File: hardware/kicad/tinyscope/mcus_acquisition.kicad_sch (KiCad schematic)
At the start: 30 parts, among them J5 STM32H743, Q2 NMOS, SW1 SW_SPST, U12 STM32H743VITx, X1 25MHz, X2 32k768

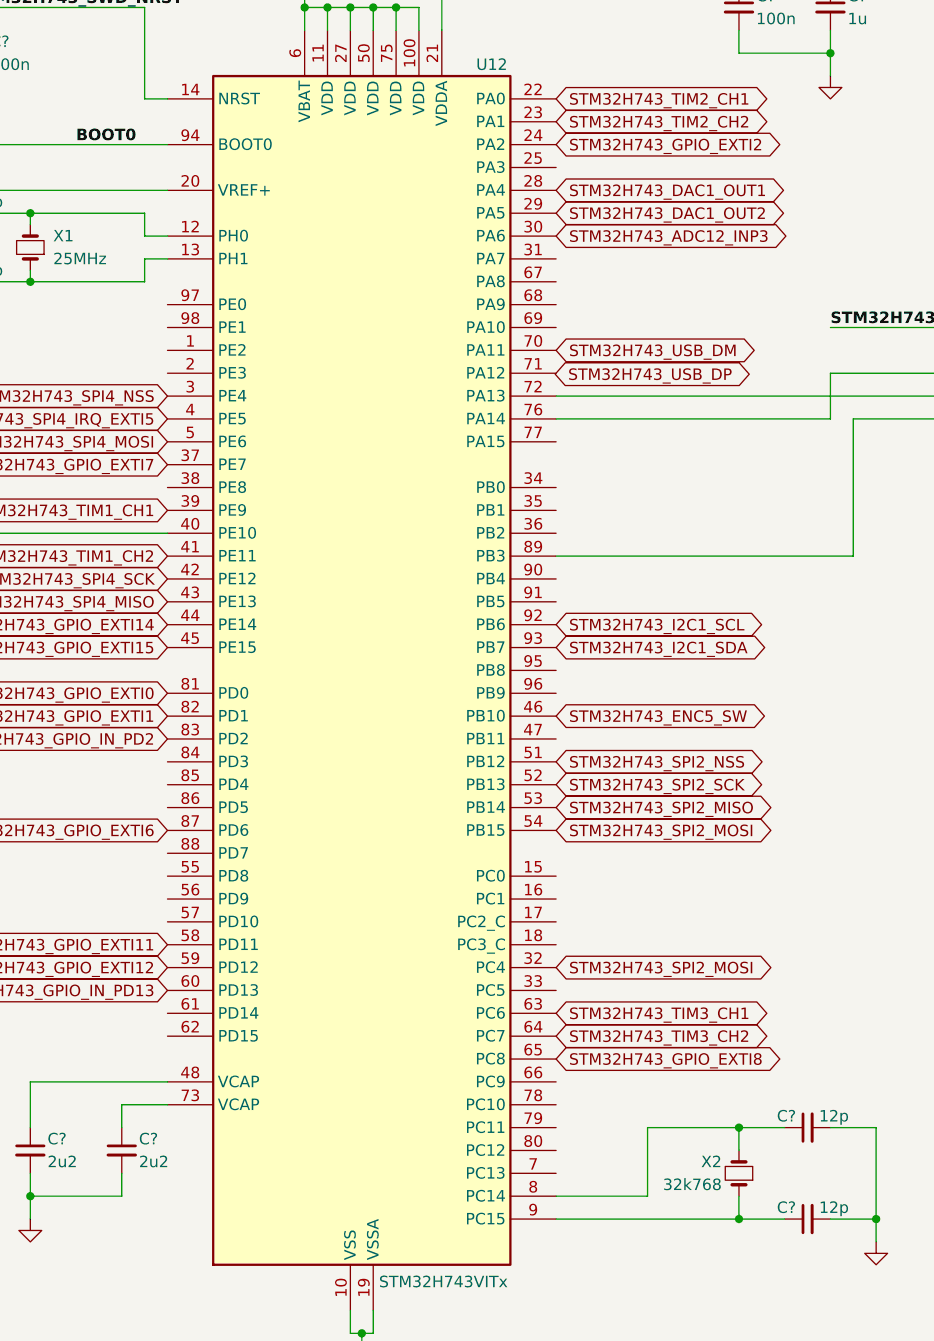
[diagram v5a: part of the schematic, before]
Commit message: feat: hardware: Adds no-connection flags for acquisition mcu
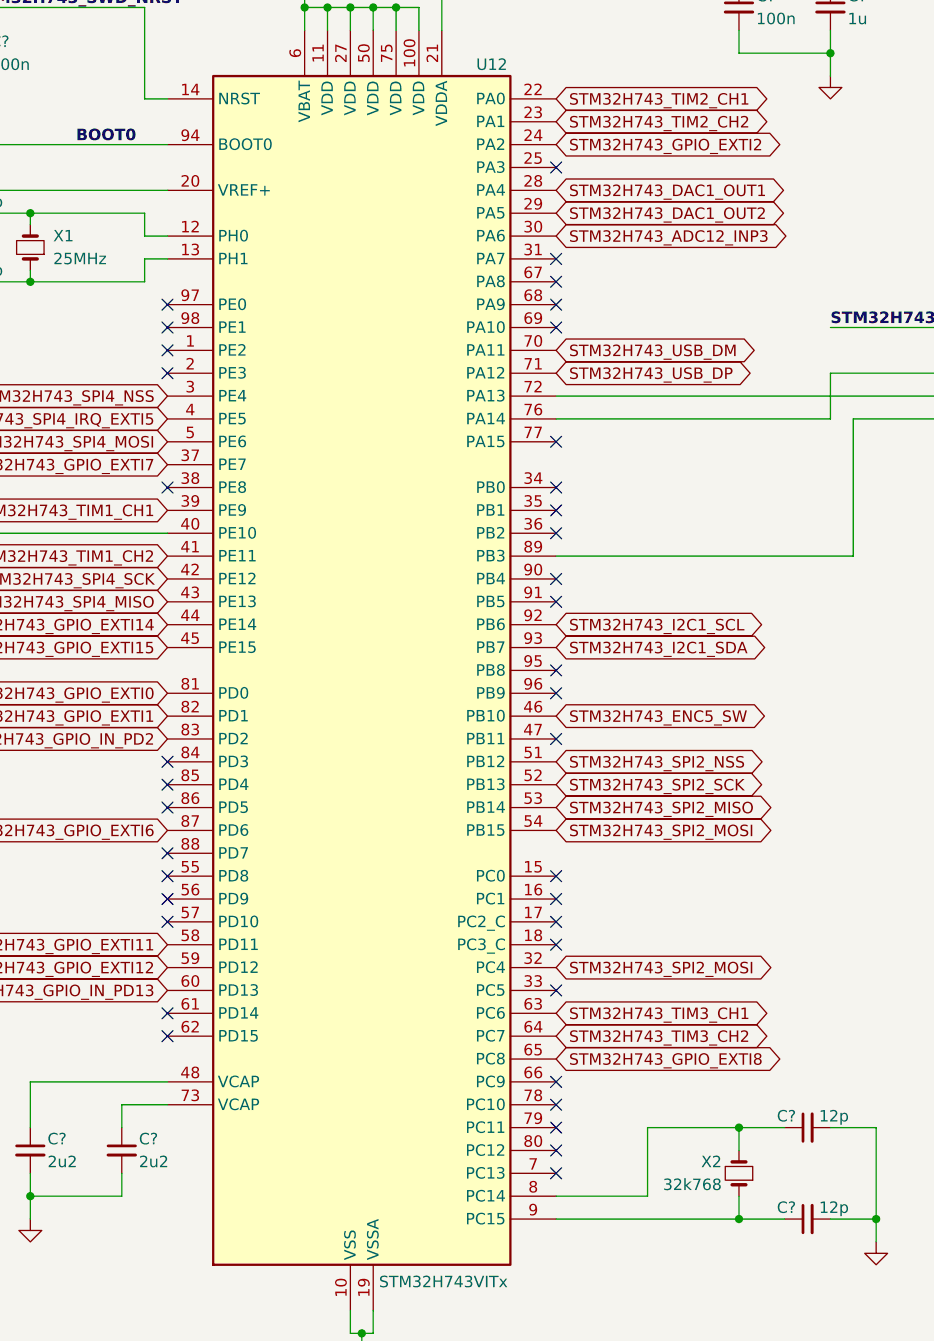
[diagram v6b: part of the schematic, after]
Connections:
- net STM32H743_USB_DP: now also U12.71 (PA12)
- no-connect marks 0 -> 38
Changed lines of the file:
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@@
   (junction (at 104.14 20.32) (diameter 0) (color 0 0 0 0)
   )
+  (no_connect (at 177.8 124.46))
+  (no_connect (at 134.62 66.04))
+  (no_connect (at 177.8 129.54))
+  (no_connect (at 134.62 109.22))
+  (no_connect (at 134.62 121.92))
+  (no_connect (at 134.62 63.5))
+  (no_connect (at 177.8 152.4))
+  (no_connect (at 177.8 55.88))
+  (no_connect (at 177.8 91.44))
+  (no_connect (at 177.8 88.9))
+  (no_connect (at 177.8 147.32))
+  (no_connect (at 177.8 53.34))
+  (no_connect (at 177.8 43.18))
+  (no_connect (at 134.62 137.16))
+  (no_connect (at 134.62 139.7))
+  (no_connect (at 177.8 81.28))
+  (no_connect (at 177.8 154.94))
+  (no_connect (at 177.8 83.82))
+  (no_connect (at 177.8 99.06))
+  (no_connect (at 134.62 78.74))
+  (no_connect (at 177.8 60.96))
+  (no_connect (at 134.62 58.42))
+  (no_connect (at 134.62 114.3))
+  (no_connect (at 177.8 106.68))
+  (no_connect (at 177.8 144.78))
+  (no_connect (at 177.8 149.86))
+  (no_connect (at 177.8 134.62))
+  (no_connect (at 134.62 111.76))
+  (no_connect (at 134.62 127))
+  (no_connect (at 177.8 101.6))
+  (no_connect (at 177.8 121.92))
+  (no_connect (at 177.8 73.66))
+  (no_connect (at 134.62 119.38))
+  (no_connect (at 134.62 124.46))
+  (no_connect (at 177.8 58.42))
+  (no_connect (at 177.8 127))
+  (no_connect (at 177.8 78.74))
+  (no_connect (at 134.62 60.96))
   (wire (pts (xy 63.5 30.48) (xy 63.5 27.94))
     (stroke (width 0) (type default))
@@
     )
   )
-  (global_label "STM32H743_USB_DP" (shape bidirectional) (at 177.6997 66.1468 0) (fields_autoplaced)
-    (effects (font (size 1.27 1.27)) (justify left))
-    (property "Intersheetrefs" "${INTERSHEET_REFS}" (at 201.0085 66.1468 0)
-      (effects (font (size 1.27 1.27)) (justify left) hide)
-    )
+  (global_label "STM32H743_USB_DP" (shape bidirectional) (at 177.8 66.04 0) (fields_autoplaced)
+    (effects (font (size 1.27 1.27)) (justify left))
+    (property "Intersheetrefs" "${INTERSHEET_REFS}" (at 201.1088 66.04 0)
+      (effects (font (size 1.27 1.27)) (justify left) hide)
+    )

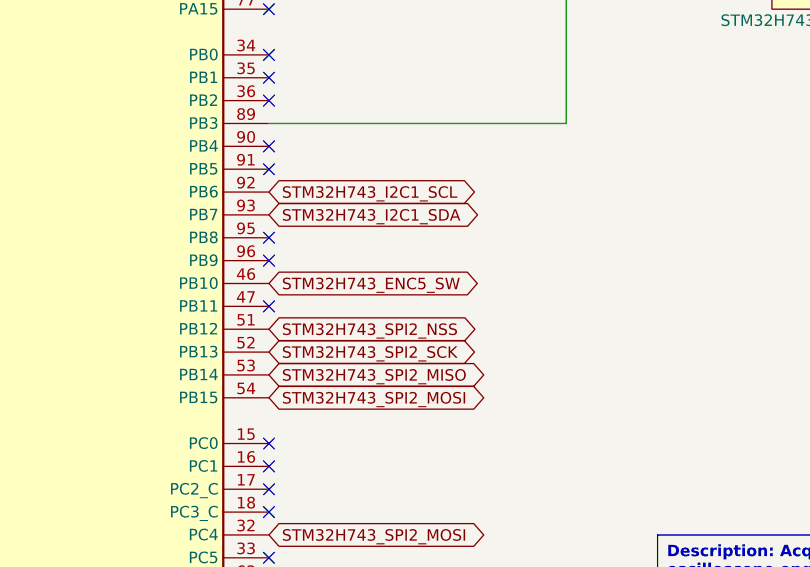
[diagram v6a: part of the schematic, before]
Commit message: feat: hardware: Add global labels on power and charging, and regulation and rails subschematics
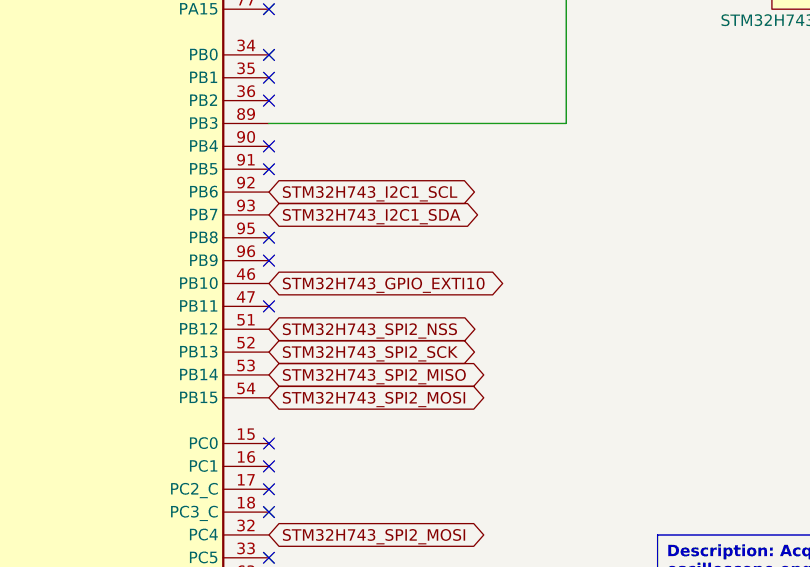
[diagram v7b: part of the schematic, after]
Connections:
- net STM32H743_ENC5_SW renamed STM32H743_GPIO_EXTI10
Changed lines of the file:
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@@
     )
   )
-  (global_label "STM32H743_ENC5_SW" (shape bidirectional) (at 177.8 104.14 0) (fields_autoplaced)
+  (global_label "STM32H743_GPIO_EXTI10" (shape bidirectional) (at 177.8 104.14 0) (fields_autoplaced)
     (effects (font (size 1.27 1.27)) (justify left))
-    (property "Intersheetrefs" "${INTERSHEET_REFS}" (at 202.3787 104.14 0)
+    (property "Intersheetrefs" "${INTERSHEET_REFS}" (at 205.584 104.14 0)
       (effects (font (size 1.27 1.27)) (justify left) hide)
     )

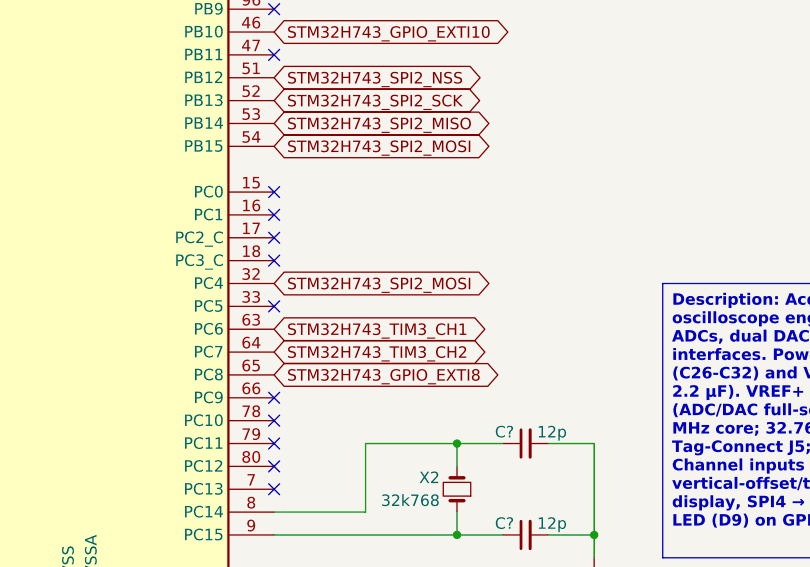
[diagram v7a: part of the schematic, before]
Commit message: fix: hardware: Solves electrical rules warnings and errors #8
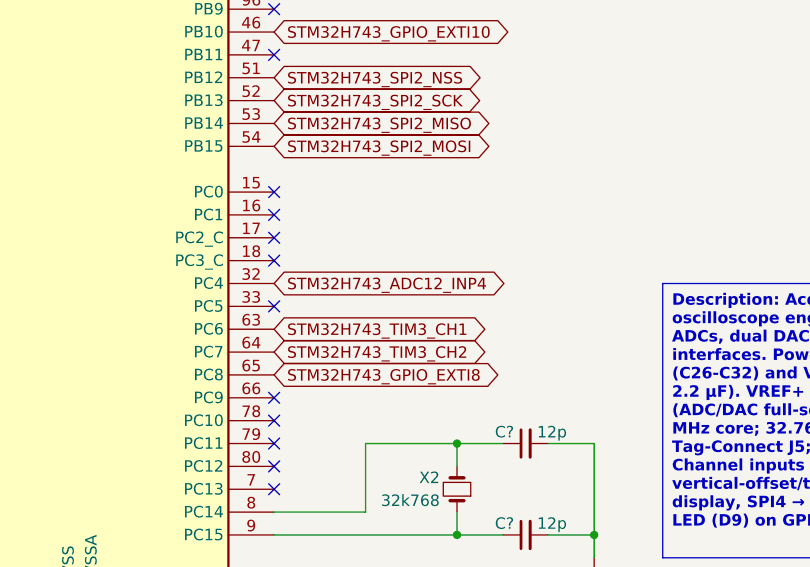
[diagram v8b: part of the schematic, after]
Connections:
- net STM32H743_SPI2_MOSI: no longer U12.32 (PC4)
- new net STM32H743_ADC12_INP4: U12.32 (PC4)
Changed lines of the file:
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@@
     )
   )
-  (global_label "STM32H743_SPI2_MOSI" (shape bidirectional) (at 177.8 132.08 0) (fields_autoplaced)
+  (global_label "STM32H743_ADC12_INP4" (shape bidirectional) (at 177.8 132.08 0) (fields_autoplaced)
     (effects (font (size 1.27 1.27)) (justify left))
-    (property "Intersheetrefs" "${INTERSHEET_REFS}" (at 203.6488 132.08 0)
+    (property "Intersheetrefs" "${INTERSHEET_REFS}" (at 205.2212 132.08 0)
       (effects (font (size 1.27 1.27)) (justify left) hide)
     )
